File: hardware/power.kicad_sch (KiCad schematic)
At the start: 19 parts, among them U12 RT5789, U13 MAX8881EUT33+T

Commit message: fixing submodule
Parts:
- removed D6: MBR0540, LED_SMD:LED_0603_1608Metric, symbol Device:D_Zener_Small_Filled
- removed D7: LED_Small_Filled, LED_SMD:LED_0603_1608Metric, symbol Device:LED_Small_Filled
- removed R41: 1k, Resistor_SMD:R_0402_1005Metric, symbol Device:R_Small
- added D5: MBR0540, LED_SMD:LED_0603_1608Metric, symbol Device:D_Zener_Small_Filled
- added D6: LED_Small_Filled, LED_SMD:LED_0603_1608Metric, symbol Device:LED_Small_Filled
- added R10: 1k, Resistor_SMD:R_0402_1005Metric, symbol Device:R_Small
- added R20: 0, Resistor_SMD:R_0805_2012Metric, symbol Device:R_Small
- added TP10: SNS_CORE-, symbol Connector:TestPoint
- added TP3: SNS_DISP+, symbol Connector:TestPoint
- added TP4: SNS_DISP-, symbol Connector:TestPoint
- added TP5: SNS_AUX+, symbol Connector:TestPoint
- added TP6: SNS_CORE+, symbol Connector:TestPoint
- added TP9: SNS_AUX-, symbol Connector:TestPoint
- R40, R43: footprint Resistor_SMD:R_0603_1608Metric_Pad0.98x0.95mm_HandSolder -> Resistor_SMD:R_0805_2012Metric
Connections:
- net 3V3_CORE: now also TP10.1
- net BOOTSTRAP: now also D5.2 (A)
- net GND: now also R10.1
- net VDD_AUX_3V3: now also TP9.1
- net VDD_SYS_3V3: now also TP5.1; no longer C47.1, C48.1, C49.1, L4.2, R36.1, R37.1, R40.1, U12.5 (VOUT)
- net PWR_CTRL.CORE_EN: no longer names the net of R36.2
- net PWR_CTRL.CORE_EN: now also C47.1, C48.1, C49.1, L4.2, R37.1, R40.1, U12.5 (VOUT), D6.2 (A), TP6.1; no longer U12.8 (EN)
- new net: R20.1, TP3.1
- new net: D6.1 (K), R10.2
- new net POWER_EN: D5.1 (K), R36.1, U12.8 (EN)
- new net VDD_DISP_3V3: R20.2, TP4.1
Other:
- note added: "B2B, WS2812"
- note added: "Bootstrap, GPS"
- note added: "Button Control"
- note added: "ESP32"
- note added: "MCU Control"
- note added: "Sensors, uSD, GPS"
- moved on the sheet: C43, C44, C45, C46, C47, C48, C49, L4, R36, R37, R38, R39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

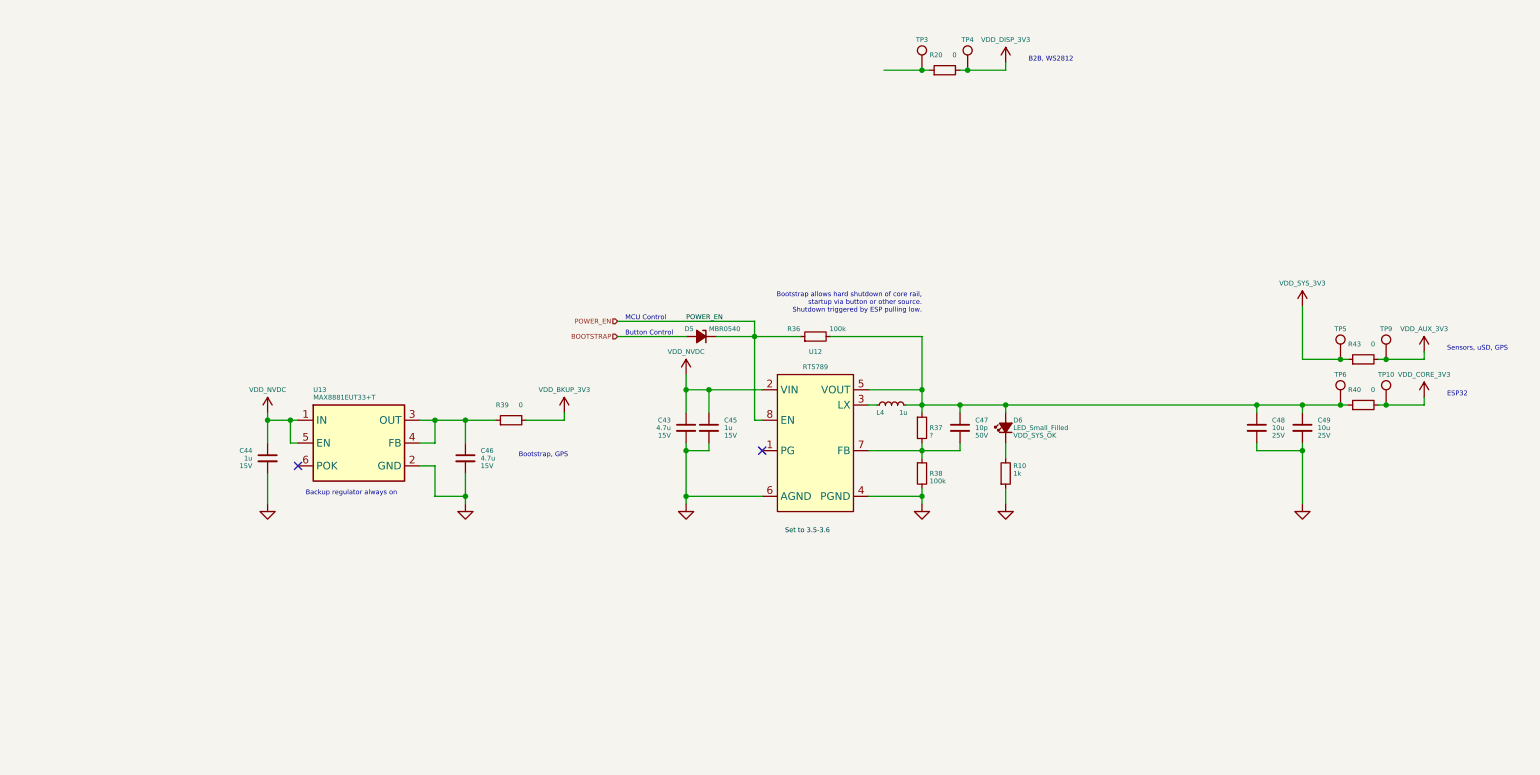
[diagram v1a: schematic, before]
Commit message: schematic tidy up, component placement, shielding investigation
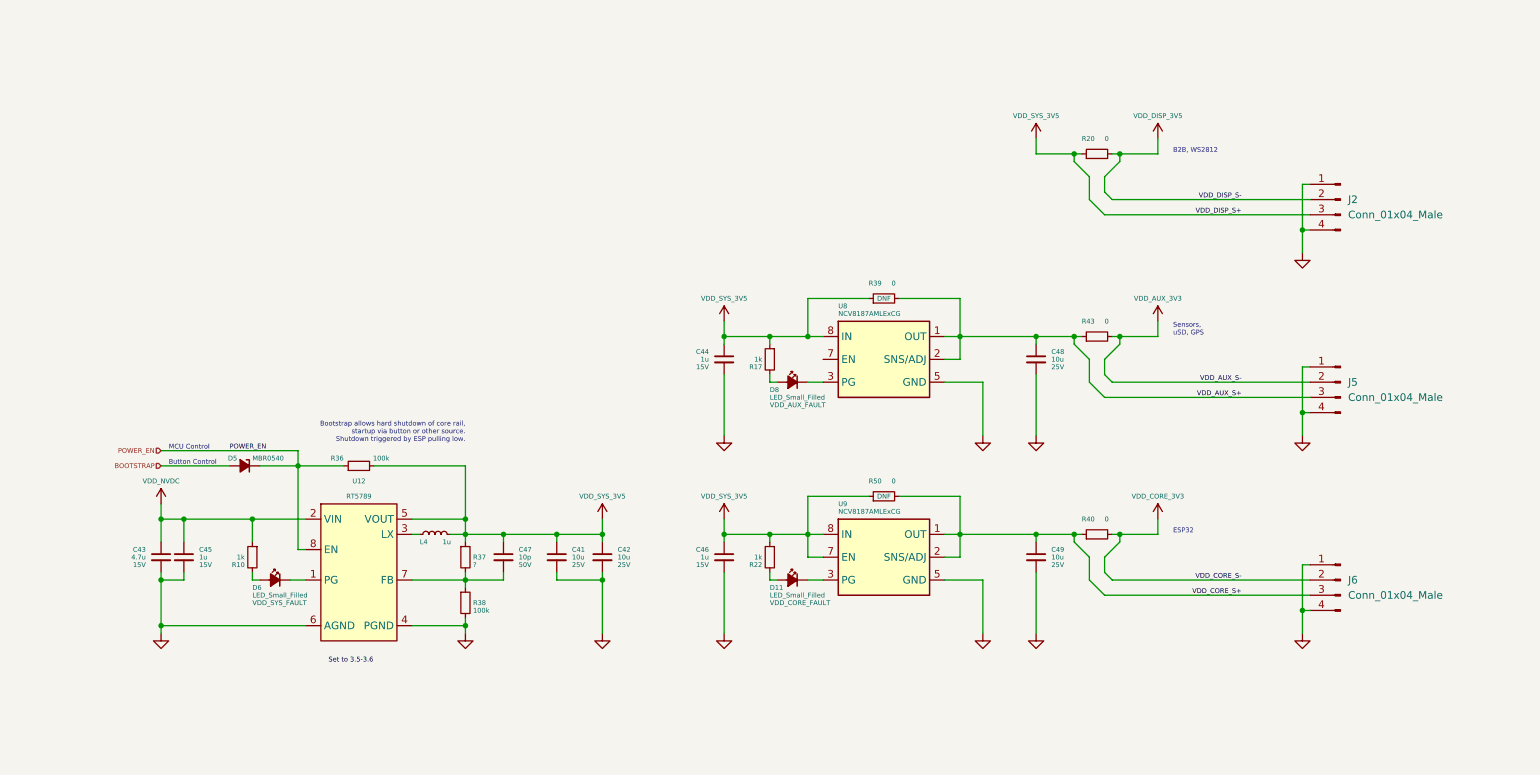
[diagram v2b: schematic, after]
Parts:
- removed TP10: SNS_CORE-, symbol Connector:TestPoint
- removed TP3: SNS_DISP+, symbol Connector:TestPoint
- removed TP4: SNS_DISP-, symbol Connector:TestPoint
- removed TP5: SNS_AUX+, symbol Connector:TestPoint
- removed TP6: SNS_CORE+, symbol Connector:TestPoint
- removed TP9: SNS_AUX-, symbol Connector:TestPoint
- removed U13: MAX8881EUT33+T, Package_TO_SOT_SMD:SOT-23-6, symbol bt_PMIC_Linear:MAX8881EUT33+T
- added C41, C42: 10u, Capacitor_SMD:C_0805_2012Metric, symbol Device:C_Small
- added D11, D8: LED_Small_Filled, LED_SMD:LED_0603_1608Metric, symbol Device:LED_Small_Filled
- added J2, J5, J6: Conn_01x04_Male, Connector_PinHeader_1.00mm:PinHeader_1x04_P1.00mm_Vertical, symbol Connector:Conn_01x04_Male
- added R17, R22: 1k, Resistor_SMD:R_0402_1005Metric, symbol Device:R_Small
- added R50: 0, Resistor_SMD:R_0805_2012Metric, symbol Device:R_Small
- added U8, U9: NCV8187AMLExCG, Package_DFN_QFN:DFN-8-1EP_3x3mm_P0.65mm_EP1.55x2.4mm, symbol bt_PMIC_Linear:NCV8187AMLExCG
- C46: value 4.7u -> 1u
- D6: Label VDD_SYS_OK -> VDD_SYS_FAULT
- R39: footprint Resistor_SMD:R_0603_1608Metric_Pad0.98x0.95mm_HandSolder -> Resistor_SMD:R_0805_2012Metric; DNF (none) -> DNF
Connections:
- net VDD_SYS_3V3 is gone; now on net VDD_AUX_S+: R43.1
- net 3V3_CORE: now also J6.2 (Pin_2)
- net GND: now also C41.2, C42.2, J2.1 (Pin_1), J2.4 (Pin_4), J5.1 (Pin_1), J5.4 (Pin_4), J6.1 (Pin_1), J6.4 (Pin_4), U8.5 (GND), U8.9 (GND), U9.5 (GND), U9.9 (GND); no longer R10.1
- net VDD_AUX_3V3: now also J5.2 (Pin_2)
- net VDD_NVDC: now also R10.1; no longer C44.1
- net VDD_SYS_3V5: now reaches C47.1, L4.2, R36.2, R37.1, U12.5 (VOUT)
- net VDD_SYS_3V5: now also C44.1, C46.1, R20.1, R39.1, C41.1, C42.1, J2.3 (Pin_3), R17.1, R22.1, R50.1, U8.8 (IN), U9.7 (EN), U9.8 (IN); no longer C48.1, C49.1, D6.2 (A), R40.1
- net at R10.2: now also D6.2 (A); no longer D6.1 (K)
- net at U12.1 (PG): now also D6.1 (K)
- net VCC_BKUP_3V3 renamed VDD_AUX_S+
- net VDD_AUX_S+: now also C48.1, J5.3 (Pin_3), U8.1 (OUT), U8.2 (SNS/ADJ)
- net VDD_DISP_3V3 renamed VDD_DISP_3V5
- net VDD_DISP_3V5: now also J2.2 (Pin_2)
- new net: D11.1 (K), U9.3 (PG)
- new net: D8.1 (K), U8.3 (PG)
- new net: D11.2 (A), R22.2
- new net: D8.2 (A), R17.2
- new net VDD_CORE_S+: C49.1, J6.3 (Pin_3), R40.1, R50.2, U9.1 (OUT), U9.2 (SNS/ADJ)
- no-connect marks 2 -> 0
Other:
- note removed: "Backup regulator always on"
- note removed: "Bootstrap, GPS"
- moved on the sheet: C43, C45, C47, C49, D5, L4, R20, R36, R37, R38, R40, R43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

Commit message: minor sch tweaks, more layout, added power emc shield
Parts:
- removed J2, J5, J6: Conn_01x04_Male, Connector_PinHeader_1.00mm:PinHeader_1x04_P1.00mm_Vertical, symbol Connector:Conn_01x04_Male
- removed R39, R50: 0, Resistor_SMD:R_0805_2012Metric, symbol Device:R_Small
- C41, C42, C48, C49: footprint Capacitor_SMD:C_0805_2012Metric -> Capacitor_SMD:C_0603_1608Metric
- C44, C45, C46: footprint Capacitor_SMD:C_0603_1608Metric -> Capacitor_SMD:C_0402_1005Metric
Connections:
- net 3V3_CORE renamed VDD_CORE_3V3
- net VDD_AUX_S+: no longer names the net of C48.1, R43.1, U8.1 (OUT), U8.2 (SNS/ADJ)
- net VDD_CORE_S+: no longer names the net of C49.1, R40.1, U9.1 (OUT), U9.2 (SNS/ADJ)

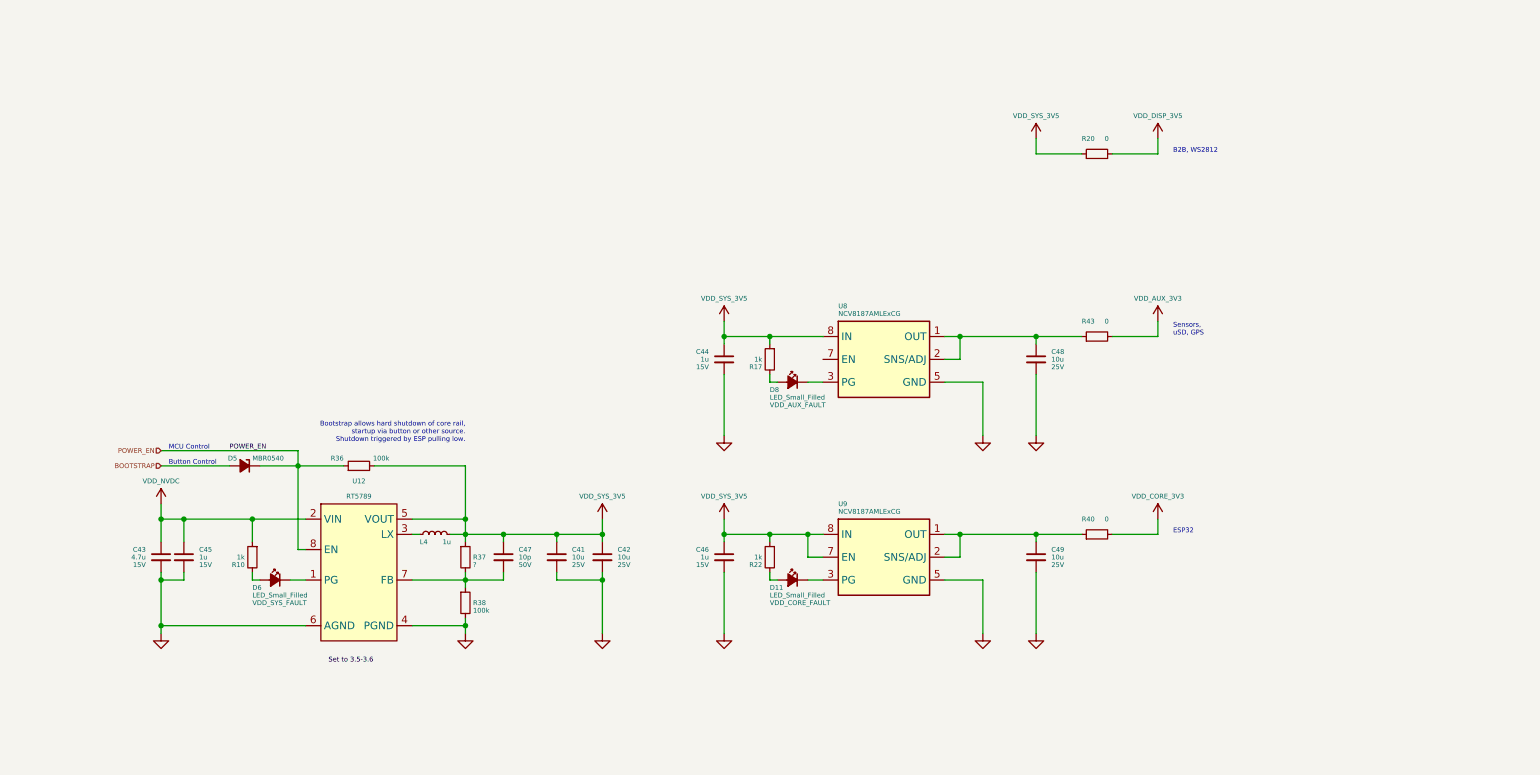
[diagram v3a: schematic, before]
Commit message: screen mock, tweaked layout easier powerplane division
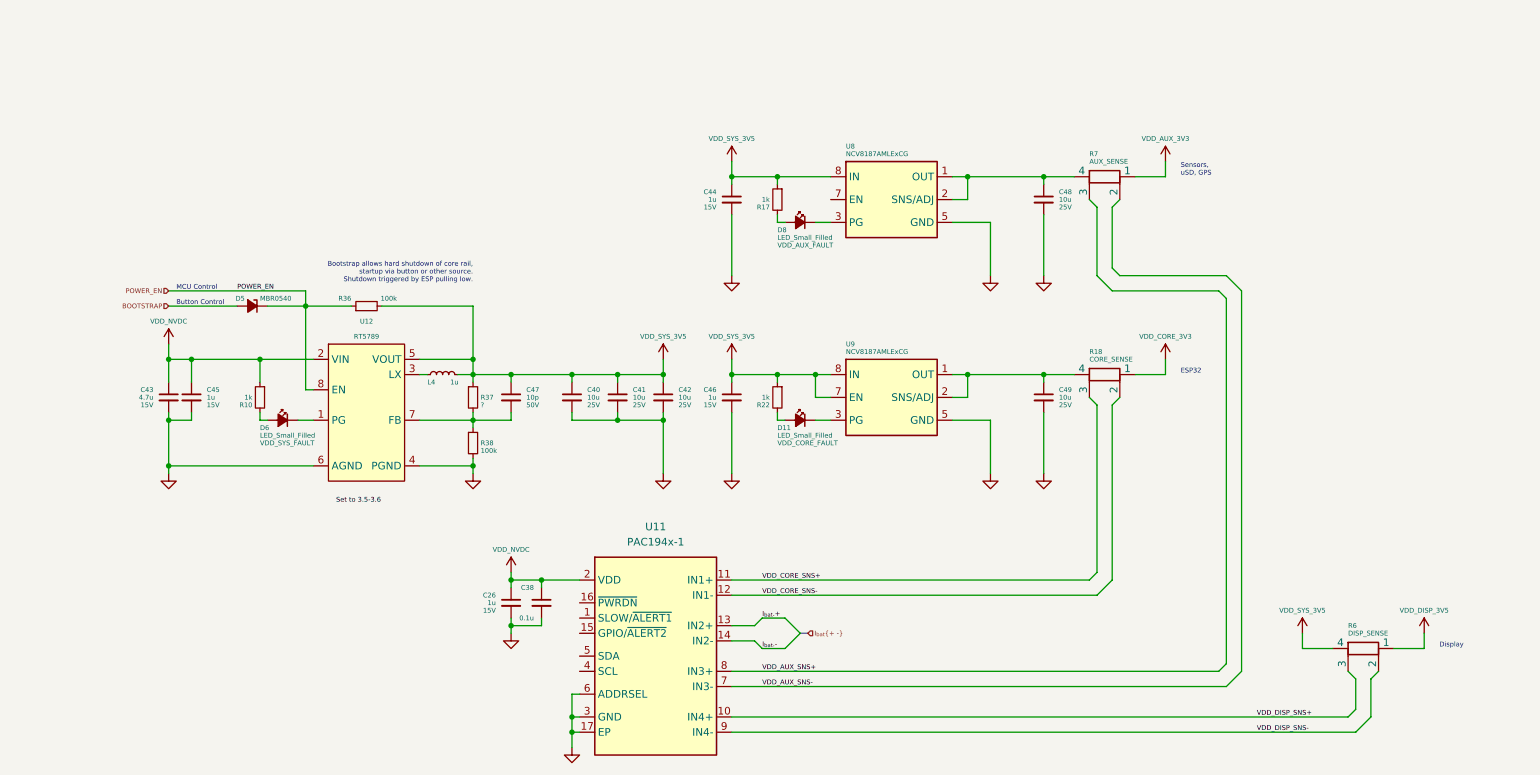
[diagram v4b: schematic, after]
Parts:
- removed R20, R40, R43: 0, Resistor_SMD:R_0805_2012Metric, symbol Device:R_Small
- added C26: 1u, Capacitor_SMD:C_0402_1005Metric, symbol Device:C_Small
- added C38: 0.1u, Capacitor_SMD:C_0402_1005Metric, symbol Device:C_Small
- added C40: 10u, Capacitor_SMD:C_0603_1608Metric, symbol Device:C_Small
- added R18: CORE_SENSE, bt_Resistor:R_0805_4WKelvin, symbol Device:R_Shunt
- added R6: DISP_SENSE, bt_Resistor:R_0805_4WKelvin, symbol Device:R_Shunt
- added R7: AUX_SENSE, bt_Resistor:R_0805_4WKelvin, symbol Device:R_Shunt
- added U11: PAC194x-1, bt_Package_QFN:VQFN-16-1EP_3x3mm_P0.5mm_EP1.2x1.2mm, symbol bt_Power_Management:PAC194x-1
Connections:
- net GND: now also C26.2, C38.2, C40.2, U11.17 (EP), U11.3 (GND), U11.6 (ADDRSEL)
- net VDD_AUX_3V3: now also R7.1
- net VDD_CORE_3V3: now also R18.1
- net VDD_DISP_3V5: now also R6.1
- net VDD_NVDC: now also C26.1, C38.1, U11.2 (VDD)
- net VDD_SYS_3V5: now also C40.1, R6.4
- net at C49.1, U9.1 (OUT), U9.2 (SNS/ADJ): now also R18.4
- net at C48.1, U8.1 (OUT), U8.2 (SNS/ADJ): now also R7.4
- new net I_{bat}.+: U11.13 (IN2+)
- new net I_{bat}.-: U11.14 (IN2-)
- new net VDD_AUX_SNS+: R7.3, U11.8 (IN3+)
- new net VDD_AUX_SNS-: R7.2, U11.7 (IN3-)
- new net VDD_CORE_SNS+: R18.3, U11.11 (IN1+)
- new net VDD_CORE_SNS-: R18.2, U11.12 (IN1-)
- new net VDD_DISP_SNS+: R6.3, U11.10 (IN4+)
- new net VDD_DISP_SNS-: R6.2, U11.9 (IN4-)
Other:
- note added: "Display"
- note removed: "B2B, WS2812"
- moved on the sheet: C41, C42, C43, C44, C45, C46, C47, C48, C49, D11, D5, D6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

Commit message: Updates
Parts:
- removed C26, C44, C45, C46: 1u, Capacitor_SMD:C_0402_1005Metric, symbol Device:C_Small
- removed C38: 0.1u, Capacitor_SMD:C_0402_1005Metric, symbol Device:C_Small
- removed C40, C41, C42, C48, C49: 10u, Capacitor_SMD:C_0603_1608Metric, symbol Device:C_Small
- removed C43: 4.7u, Capacitor_SMD:C_0603_1608Metric, symbol Device:C_Small
- removed C47: 10p, Capacitor_SMD:C_0402_1005Metric, symbol Device:C_Small
- removed D11, D6, D8: LED_Small_Filled, LED_SMD:LED_0603_1608Metric, symbol Device:LED_Small_Filled
- removed D5: MBR0540, LED_SMD:LED_0603_1608Metric, symbol Device:D_Zener_Small_Filled
- removed L4: 1u, Inductor_SMD:L_Wuerth_MAPI-2510, symbol Device:L_Small
- removed R10, R17, R22: 1k, Resistor_SMD:R_0402_1005Metric, symbol Device:R_Small
- removed R18: CORE_SENSE, bt_Resistor:R_0805_4WKelvin, symbol Device:R_Shunt
- removed R36, R38: 100k, Resistor_SMD:R_0402_1005Metric, symbol Device:R_Small
- removed R37: ?, Resistor_SMD:R_0402_1005Metric, symbol Device:R_Small
- removed R6: DISP_SENSE, bt_Resistor:R_0805_4WKelvin, symbol Device:R_Shunt
- removed R7: AUX_SENSE, bt_Resistor:R_0805_4WKelvin, symbol Device:R_Shunt
- removed U11: PAC194x-1, bt_Package_QFN:VQFN-16-1EP_3x3mm_P0.5mm_EP1.2x1.2mm, symbol bt_Power_Management:PAC194x-1
- removed U12: RT5789, Package_TO_SOT_SMD:TSOT-23-8, symbol bt_PMIC_DCDC_Buck:RT5789
- removed U8, U9: NCV8187AMLExCG, Package_DFN_QFN:DFN-8-1EP_3x3mm_P0.65mm_EP1.55x2.4mm, symbol bt_PMIC_Linear:NCV8187AMLExCG
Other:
- note removed: "Bootstrap allows hard shutdown of core rail, startup via button or other source. Shutdown triggered by ESP pulling low."
- note removed: "Button Control"
- note removed: "Display"
- note removed: "ESP32"
- note removed: "MCU Control"
- note removed: "Sensors, uSD, GPS"
